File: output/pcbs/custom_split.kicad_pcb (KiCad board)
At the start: 2 copper layers, 135.1 x 84 mm, 39 parts

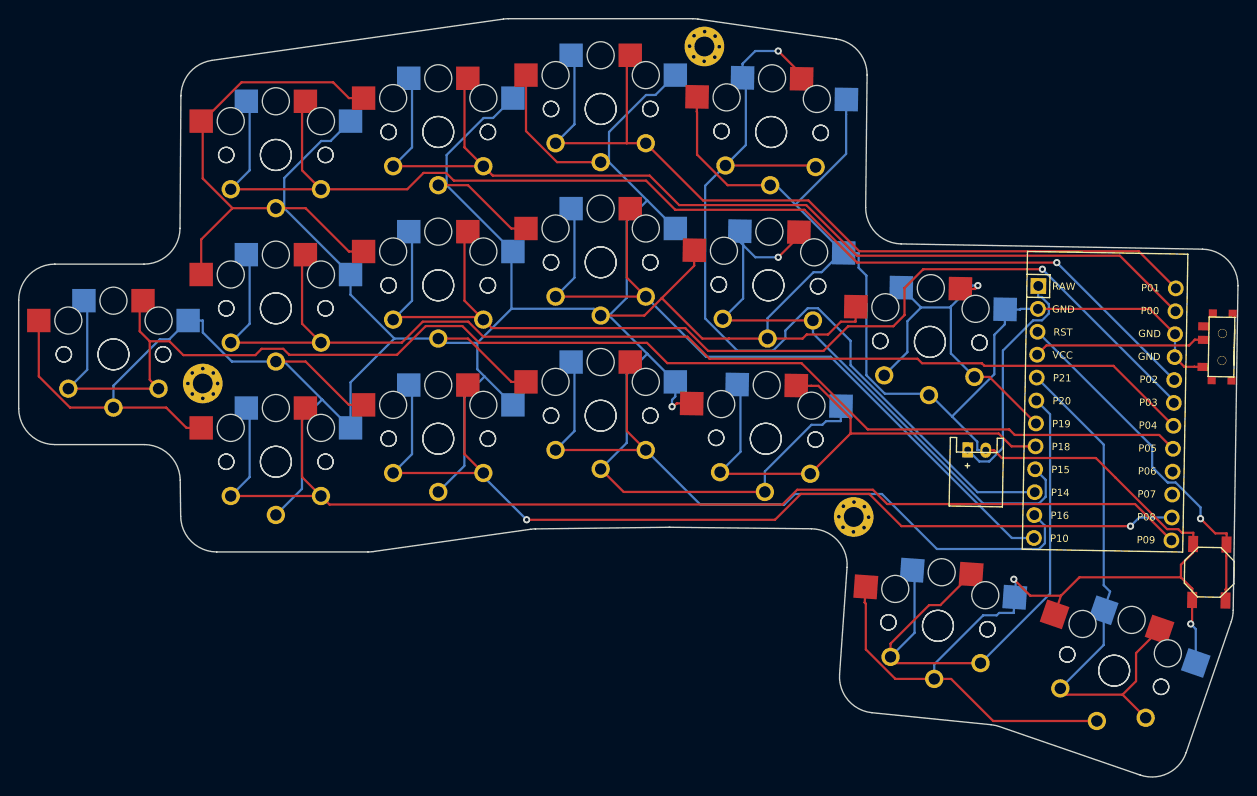
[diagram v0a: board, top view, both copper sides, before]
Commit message: changed board constraints
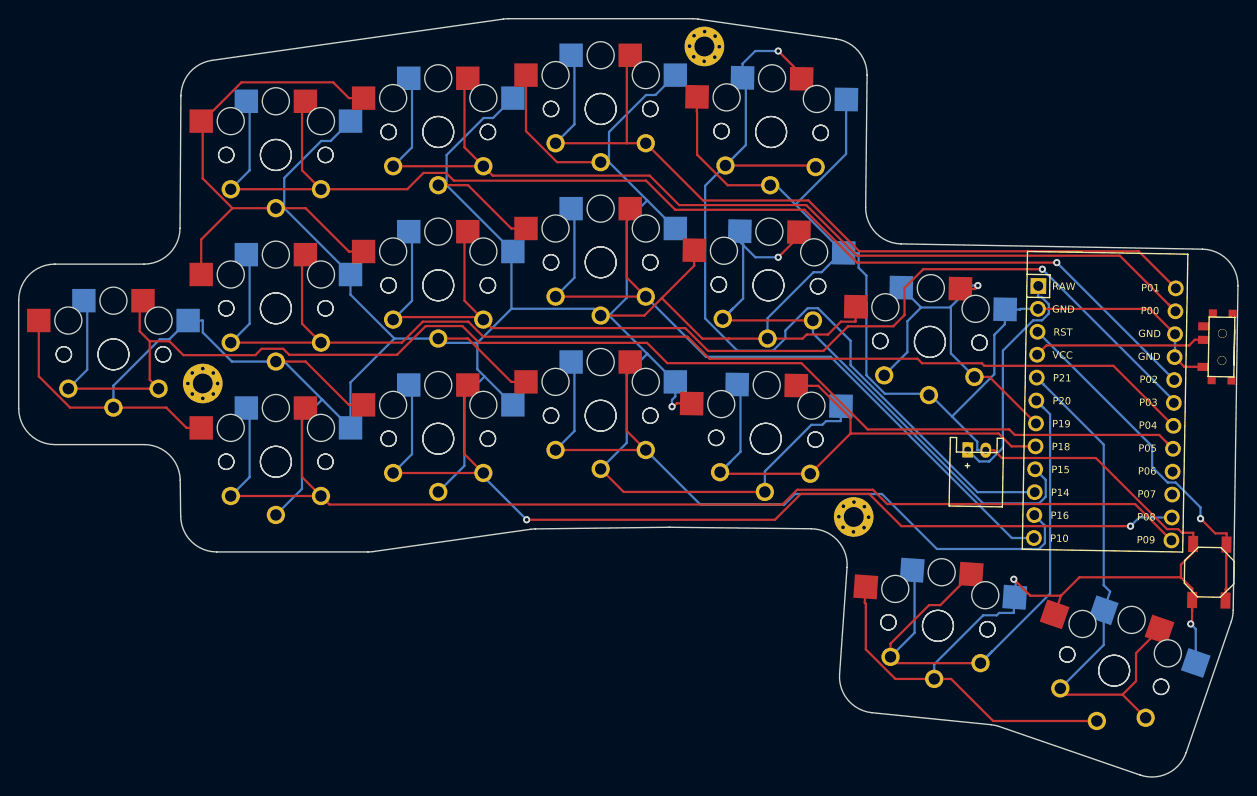
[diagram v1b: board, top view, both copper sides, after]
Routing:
- net GND: track 701.9 -> 710.4 mm
- net P20: track 67.6 -> 71.2 mm
- net P15: track 69.6 -> 72.2 mm
- net P18: track 57.5 -> 59.4 mm
- net P21: track 59.6 -> 60.8 mm
- net P0: track 114.9 -> 116.0 mm
- net P5: track 153.1 -> 154.2 mm
- net RST: track 39.8 -> 40.4 mm
- net RAW: track 26.4 -> 27.0 mm

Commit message: switched the footprint to one that didn't clip pads; no more errors in kicad
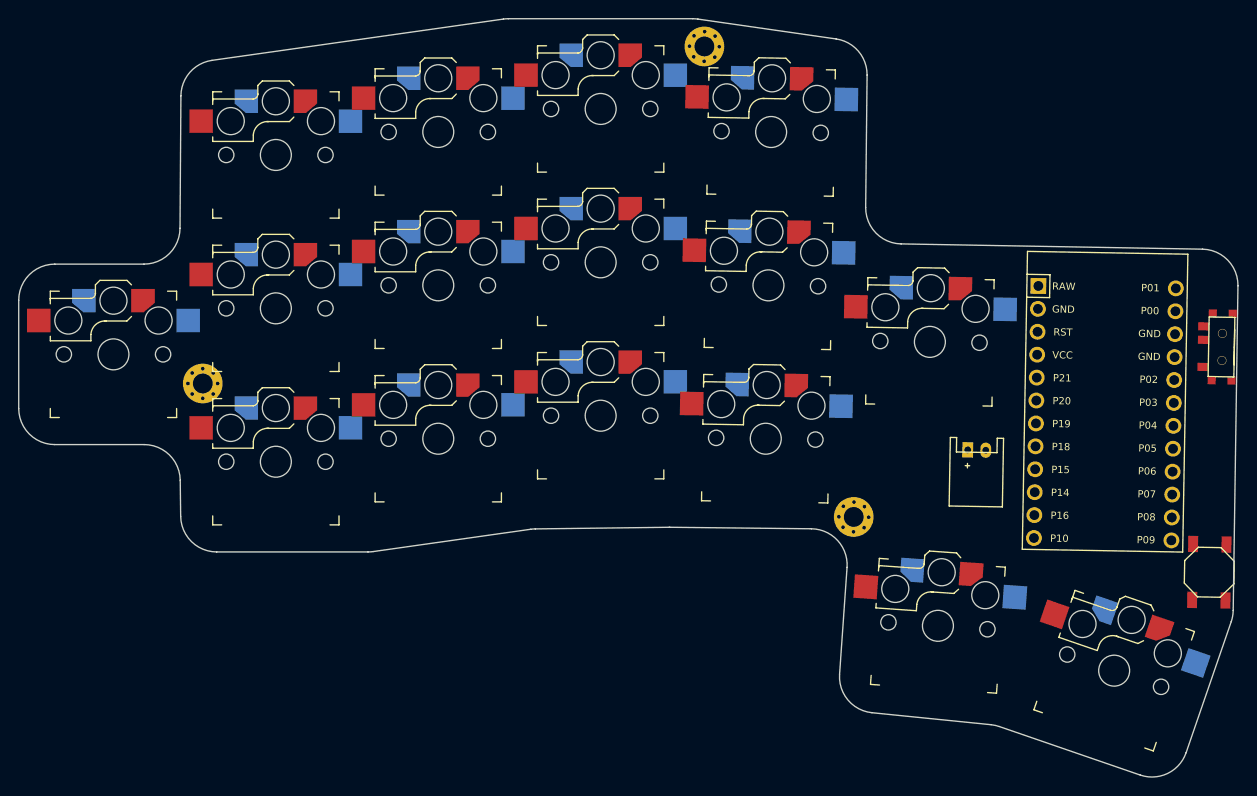
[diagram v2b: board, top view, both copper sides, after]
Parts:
- removed S17, S18, S19, S20, S21, S22, S23, S24, S25, S26, S27, S28, S29, S30, S31, S32: , PG1350
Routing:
- net GND: track 710.4 -> 0.00 mm, vias 3 -> 0
- net P5: track 154.2 -> 0.00 mm
- net P2: track 136.4 -> 0.00 mm, vias 1 -> 0
- net P4: track 131.8 -> 0.00 mm
- net P9: track 129.2 -> 0.00 mm
- net P3: track 121.5 -> 0.00 mm, vias 1 -> 0
- net P0: track 116.0 -> 0.00 mm
- net P8: track 113.3 -> 0.00 mm, vias 2 -> 0
- net P14: track 99.6 -> 0.00 mm, vias 1 -> 0
- net P1: track 96.1 -> 0.00 mm
- net P10: track 85.6 -> 0.00 mm
- net P16: track 85.2 -> 0.00 mm
- net P15: track 72.2 -> 0.00 mm, vias 1 -> 0
- net P20: track 71.2 -> 0.00 mm
- net P21: track 60.8 -> 0.00 mm
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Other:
- net class Default added: clearance 0.2, trace_width 0.25, via_dia 0.8, via_drill 0.4

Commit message: forgot to save the bp
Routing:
- net GND: track 0.00 -> 622.0 mm, vias 0 -> 4
- net P5: track 0.00 -> 129.4 mm, vias 0 -> 1
- net P2: track 0.00 -> 117.9 mm, vias 0 -> 1
- net P4: track 0.00 -> 113.0 mm, vias 0 -> 1
- net P9: track 0.00 -> 110.9 mm, vias 0 -> 1
- net P8: track 0.00 -> 99.8 mm, vias 0 -> 1
- net P0: track 0.00 -> 98.3 mm, vias 0 -> 1
- net P3: track 0.00 -> 94.7 mm, vias 0 -> 1
- net P1: track 0.00 -> 80.7 mm, vias 0 -> 1
- net P10: track 0.00 -> 80.2 mm, vias 0 -> 1
- net P14: track 0.00 -> 73.4 mm, vias 0 -> 1
- net P16: track 0.00 -> 63.7 mm, vias 0 -> 1
- net P15: track 0.00 -> 56.2 mm, vias 0 -> 1
- net RST: track 0.00 -> 39.7 mm, vias 0 -> 1
- net P19: track 0.00 -> 38.6 mm, vias 0 -> 1
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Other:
- net class Default removed

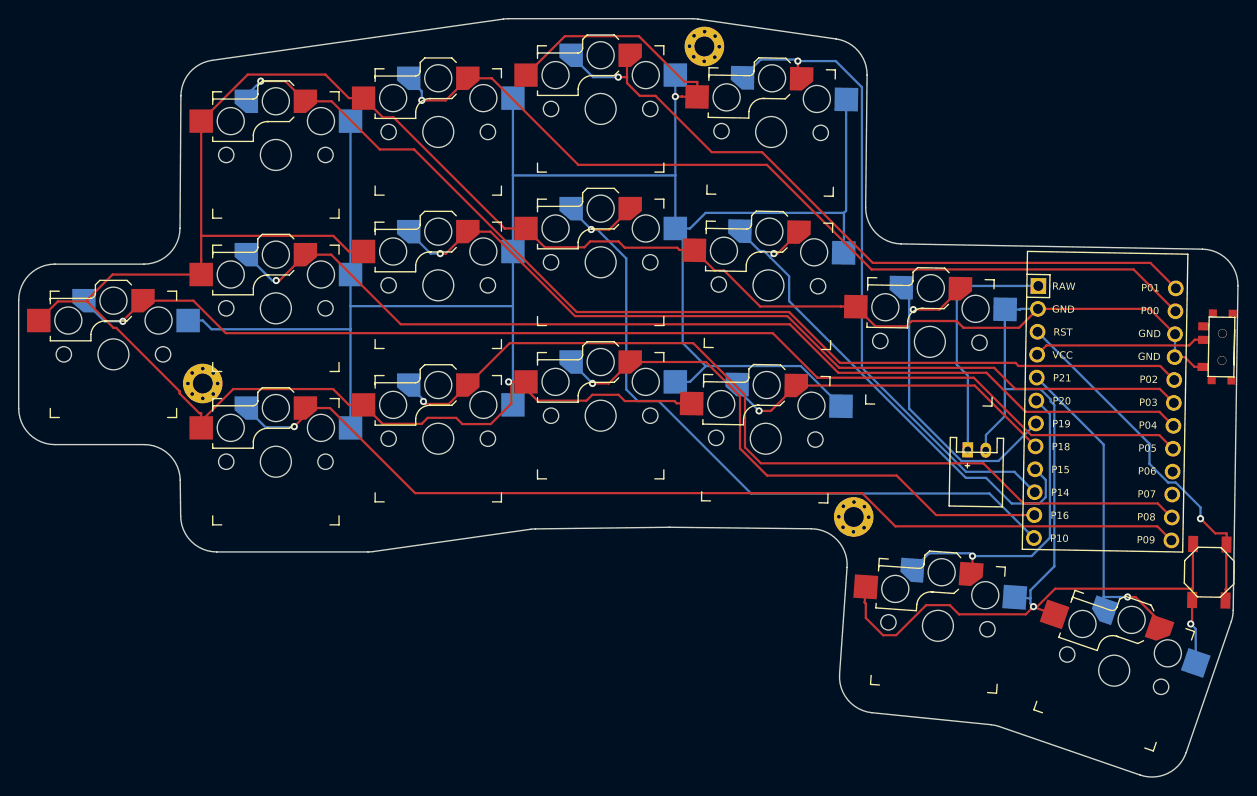
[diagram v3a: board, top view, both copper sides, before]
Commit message: added nice!nano footprint and updated the config
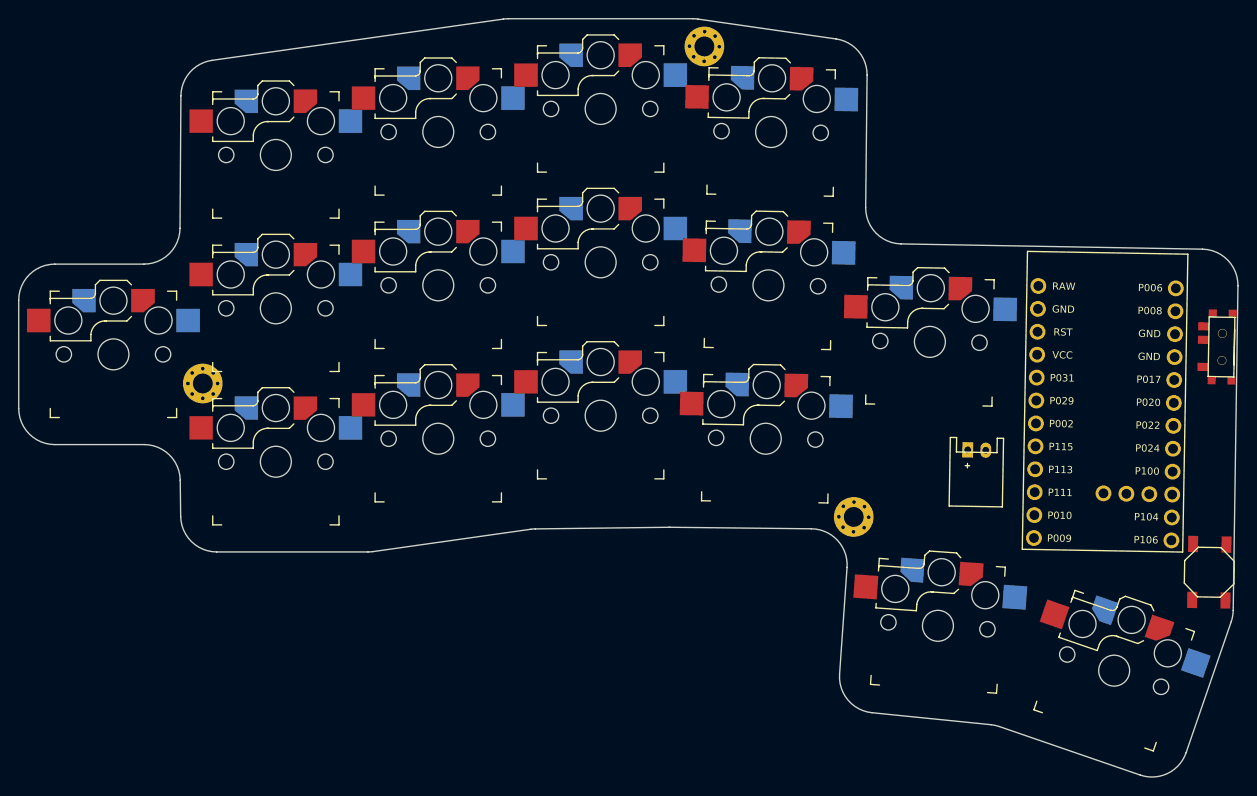
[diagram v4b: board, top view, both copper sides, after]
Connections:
- net P6 renamed P100
- net P7 renamed P011
- MCU1 pad 10: P14 -> P111
- MCU1 pad 11: P16 -> P010
- MCU1 pad 12: P10 -> P009
- MCU1 pad 13: P1 -> P006
- MCU1 pad 14: P0 -> P008
- MCU1 pad 17: P2 -> P017
- MCU1 pad 18: P3 -> P020
- MCU1 pad 19: P4 -> P022
- MCU1 pad 20: P5 -> P024
- MCU1 pad 23: P8 -> P104
- MCU1 pad 24: P9 -> P106
- MCU1 pad 5: P21 -> P031
- MCU1 pad 6: P20 -> P029
- MCU1 pad 7: P19 -> P002
- MCU1 pad 8: P18 -> P115
- MCU1 pad 9: P15 -> P113
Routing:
- net GND: track 622.0 -> 0.00 mm, vias 4 -> 0
- net P5: track 129.4 -> 0.00 mm, vias 1 -> 0
- net P2: track 117.9 -> 0.00 mm, vias 1 -> 0
- net P4: track 113.0 -> 0.00 mm, vias 1 -> 0
- net P9: track 110.9 -> 0.00 mm, vias 1 -> 0
- net P8: track 99.8 -> 0.00 mm, vias 1 -> 0
- net P0: track 98.3 -> 0.00 mm, vias 1 -> 0
- net P3: track 94.7 -> 0.00 mm, vias 1 -> 0
- net P1: track 80.7 -> 0.00 mm, vias 1 -> 0
- net P10: track 80.2 -> 0.00 mm, vias 1 -> 0
- net P14: track 73.4 -> 0.00 mm, vias 1 -> 0
- net P16: track 63.7 -> 0.00 mm, vias 1 -> 0
- net P15: track 56.2 -> 0.00 mm, vias 1 -> 0
- net RST: track 39.7 -> 0.00 mm, vias 1 -> 0
- net P19: track 38.6 -> 0.00 mm, vias 1 -> 0
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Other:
- net class Default added: clearance 0.2, trace_width 0.25, via_dia 0.8, via_drill 0.4

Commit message: renamed the pins and regenerated the nets
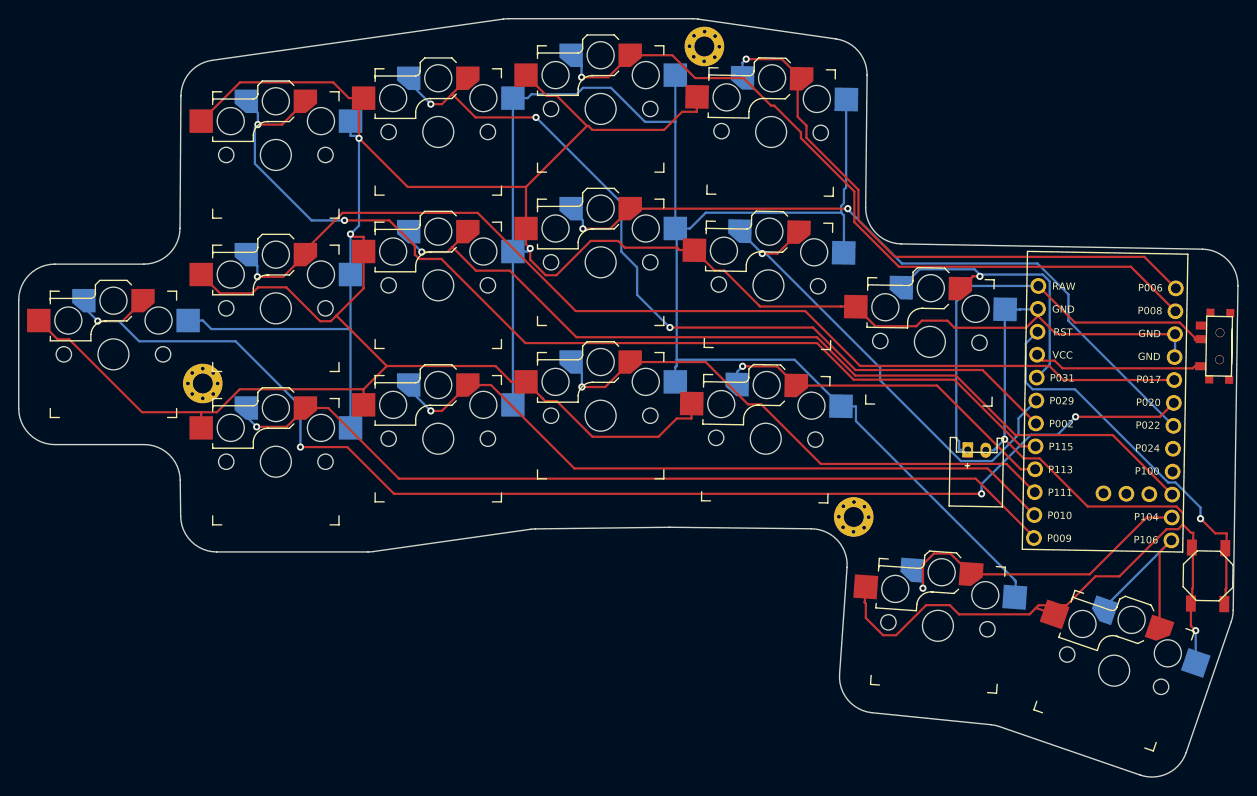
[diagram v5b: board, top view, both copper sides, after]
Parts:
- moved B1 0.42 mm to (281.3, 177.6)
- moved T1 0.28 mm to (282.6, 152.1)
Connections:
- S1 pad 1: P5 -> P020
- S10 pad 1: P1 -> P008
- S11 pad 1: P18 -> P113
- S12 pad 1: P15 -> P029
- S13 pad 1: P14 -> P006
- S14 pad 1: P19 -> P031
- S15 pad 1: P20 -> P104
- S16 pad 1: P21 -> P106
- S2 pad 1: P9 -> P009
- S3 pad 1: P4 -> P017
- S4 pad 1: P2 -> P115
- S5 pad 1: P8 -> P010
- S6 pad 1: P3 -> P011
- S7 pad 1: P0 -> P002
- S8 pad 1: P16 -> P111
- S9 pad 1: P10 -> P022
- T1 pad 1: GND -> VCC
- T1 pad 2: VCC -> RAW
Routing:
- net GND: track 0.00 -> 635.6 mm, vias 0 -> 5
- net P020: track 0.00 -> 143.5 mm, vias 0 -> 4
- net P017: track 0.00 -> 115.5 mm, vias 0 -> 1
- net P115: track 0.00 -> 114.0 mm, vias 0 -> 2
- net P011: track 0.00 -> 100.0 mm, vias 0 -> 1
- net P009: track 0.00 -> 95.6 mm, vias 0 -> 1
- net P002: track 0.00 -> 94.0 mm, vias 0 -> 3
- net P008: track 0.00 -> 83.9 mm, vias 0 -> 1
- net P022: track 0.00 -> 80.9 mm, vias 0 -> 2
- net P010: track 0.00 -> 77.9 mm, vias 0 -> 1
- net P006: track 0.00 -> 66.2 mm, vias 0 -> 1
- net P111: track 0.00 -> 60.6 mm, vias 0 -> 1
- net P029: track 0.00 -> 53.1 mm, vias 0 -> 1
- net RAW: track 0.00 -> 48.2 mm
- net RST: track 0.00 -> 43.5 mm, vias 0 -> 1
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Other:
- net class Default removed
